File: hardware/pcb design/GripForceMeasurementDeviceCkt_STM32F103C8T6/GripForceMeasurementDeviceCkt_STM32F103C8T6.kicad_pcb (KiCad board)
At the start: 2 copper layers, 60 parts, among them J1 Conn_01x32, J10 Conn_01x32, J11 Conn_01x32, J12 Conn_01x32, J13 Conn_01x32, J2 Conn_01x03, J3 Conn_01x04, J4 Conn_02x03_CC, J5 Conn_01x32, J6 Conn_01x32, J7 Conn_01x32, J8 Conn_01x32, J9 Conn_01x32, P1 USB_C_Plug_USB2.0, U1 STM32F103C8Tx, U10 ADG732BSUZ, U11 ADG732BSUZ, U12 ADG732BSUZ, U13 ADG732BSUZ, U2 FT232RL, U3 ADG732BSUZ, U4 ADG732BSUZ, U5 LM358, U6 ADG732BSUZ, U7 ADG732BSUZ, U8 ADG732BSUZ, U9 ADG732BSUZ, Y1 8MHz

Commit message: complete schemetic design. working on PCB
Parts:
- removed the J10 at (87.5, 145.8)
- removed the J6 at (232.8, 56.5)
- added J14: Conn_01x32, Connector_FFC-FPC:Hirose_FH12-32S-0.5SH_1x32-1MP_P0.50mm_Horizontal, B.Cu at (39.2, 118.1)
- added J15: Conn_01x32, Connector_FFC-FPC:Hirose_FH12-32S-0.5SH_1x32-1MP_P0.50mm_Horizontal, B.Cu at (64.6, 118.1)
- added J16: Conn_01x32, Connector_FFC-FPC:Hirose_FH12-32S-0.5SH_1x32-1MP_P0.50mm_Horizontal, B.Cu at (90.1, 118.1)
- added J17: Conn_01x32, Connector_FFC-FPC:Hirose_FH12-32S-0.5SH_1x32-1MP_P0.50mm_Horizontal, B.Cu at (115.2, 118.1)
- added J19: Power_Conn, Connector_PinHeader_2.54mm:PinHeader_1x03_P2.54mm_Vertical, F.Cu at (35.6, 58.2)
- added J3: TX_Conn, Connector_PinHeader_2.54mm:PinHeader_1x03_P2.54mm_Vertical, F.Cu at (111.3, 65.8)
- added J4: Bluetooth_Module_HLK_B40_(Customized), Connector_PinSocket_2.54mm:PinSocket_1x06_P2.54mm_Vertical, F.Cu at (119.3, 66.9)
- added U1: ESP32-C3-Mini, RF_WiFi:ESP32-C3-Mini-through-hole, F.Cu at (163.1, 65.0)
- C13: renamed from C9; moved to B.Cu
- C14: renamed from C10; moved to B.Cu
- C20: renamed from C24; moved to B.Cu
- C21: renamed from C22; moved to B.Cu
- C22: renamed from C23; moved to B.Cu
- C23: renamed from C21; moved to B.Cu
- C24: renamed from C16; moved to B.Cu
- J1: value Conn_01x32 -> RX_Conn; footprint Connector_FFC-FPC:TE_3-1734839-2_1x32-1MP_P0.5mm_Horizontal -> Connector_PinHeader_2.54mm:PinHeader_1x03_P2.54mm_Vertical
- J10: renamed from J5; footprint Connector_FFC-FPC:TE_3-1734839-2_1x32-1MP_P0.5mm_Horizontal -> Connector_FFC-FPC:Hirose_FH12-32S-0.5SH_1x32-1MP_P0.50mm_Horizontal
- J11, J12, J8, J9: footprint Connector_FFC-FPC:TE_3-1734839-2_1x32-1MP_P0.5mm_Horizontal -> Connector_FFC-FPC:Hirose_FH12-32S-0.5SH_1x32-1MP_P0.50mm_Horizontal
- J13: footprint Connector_FFC-FPC:TE_3-1734839-2_1x32-1MP_P0.5mm_Horizontal -> Connector_FFC-FPC:Hirose_FH12-32S-0.5SH_1x32-1MP_P0.50mm_Horizontal; moved to B.Cu
- J2: renamed from J4; value Conn_02x03_CC -> Boot_Conn
- J5: renamed from J3; value Conn_01x04 -> SWD
- J7: value Conn_01x32 -> Gyro_Sensor_ICM_20948_SparkFun_Module; footprint Connector_FFC-FPC:TE_3-1734839-2_1x32-1MP_P0.5mm_Horizontal -> Connector_PinSocket_2.54mm:PinSocket_1x06_P2.54mm_Vertical
- U10: renamed from U13; moved to B.Cu
- U11, U12: moved to B.Cu
- U13: renamed from U10; moved to B.Cu
- moved D1 244.7 mm to (36.5, 62.2), turned to 180 degrees
- moved U2 241.9 mm to (32.4, 79.5), turned to 90 degrees
- moved U3 241.8 mm to (32.1, 90.4), turned to 90 degrees
- moved RV1 237.6 mm to (39.5, 87.9), turned to 90 degrees
- moved P1 236.6 mm to (27.7, 66.8), turned to -90 degrees
- moved J6 228.2 mm to (26.2, 93.1), turned to 180 degrees
- moved C9 227.6 mm to (40.7, 63.7), turned to -90 degrees
- moved R4 226.1 mm to (45.1, 86.6), turned to -90 degrees
- moved U13 224.3 mm to (39.2, 108.0)
- moved L1 224.3 mm to (45.1, 62.2)
- moved C11 222.2 mm to (44.7, 68.5), turned to 180 degrees
- moved R3 222.1 mm to (34.0, 73.2), turned to 180 degrees
- moved C1 220.2 mm to (30.8, 73.2)
- moved R1 219.9 mm to (37.0, 65.4)
- moved C13 218.1 mm to (66.6, 67.7), turned to 180 degrees
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- renumbered C14 to C1, C11 to C10, C12 to C11, C8 to C12, C20 to C15, C15 to C16, C1 to C2, C2 to C3, C3 to C4, C4 to C5, C5 to C6, C6 to C7, C7 to C8, C13 to C9, J2 to J6, R2 to R1, R1 to R2, U4 to U14, U5 to U3, U1 to U4, U9 to U5, U3 to U6, U6 to U7, U7 to U8, U8 to U9
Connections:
- J1 pad 1: ROW_L_1 -> TX_BTH
- J1 pad 2: ROW_L_2 -> RX
- J1 pad 3: ROW_L_3 -> TX_USB
- J11 pad 1: /COL_R_2.S1 -> /COL_L_2.S17
- J11 pad 10: /COL_R_2.S10 -> /COL_L_2.S26
- J11 pad 11: /COL_R_2.S11 -> /COL_L_2.S27
- J11 pad 12: /COL_R_2.S12 -> /COL_L_2.S28
- J11 pad 13: /COL_R_2.S13 -> /COL_L_2.S29
- J11 pad 14: /COL_R_2.S14 -> /COL_L_2.S30
- J11 pad 15: /COL_R_2.S15 -> /COL_L_2.S31
- J11 pad 16: /COL_R_2.S16 -> /COL_L_2.S32
- J11 pad 17: /COL_R_2.S32 -> /COL_L_2.S16
- J11 pad 18: /COL_R_2.S31 -> /COL_L_2.S15
- J11 pad 19: /COL_R_2.S30 -> /COL_L_2.S14
- J11 pad 2: /COL_R_2.S2 -> /COL_L_2.S18
- J11 pad 20: /COL_R_2.S29 -> /COL_L_2.S13
- J11 pad 21: /COL_R_2.S28 -> /COL_L_2.S12
- J11 pad 22: /COL_R_2.S27 -> /COL_L_2.S11
- J11 pad 23: /COL_R_2.S26 -> /COL_L_2.S10
- J11 pad 24: /COL_R_2.S25 -> /COL_L_2.S9
- J11 pad 25: /COL_R_2.S24 -> /COL_L_2.S8
- J11 pad 26: /COL_R_2.S23 -> /COL_L_2.S7
- J11 pad 27: /COL_R_2.S22 -> /COL_L_2.S6
- J11 pad 28: /COL_R_2.S21 -> /COL_L_2.S5
- J11 pad 29: /COL_R_2.S20 -> /COL_L_2.S4
- J11 pad 3: /COL_R_2.S3 -> /COL_L_2.S19
- J11 pad 30: /COL_R_2.S19 -> /COL_L_2.S3
- J11 pad 31: /COL_R_2.S18 -> /COL_L_2.S2
- J11 pad 32: /COL_R_2.S17 -> /COL_L_2.S1
- J11 pad 4: /COL_R_2.S4 -> /COL_L_2.S20
- J11 pad 5: /COL_R_2.S5 -> /COL_L_2.S21
- J11 pad 6: /COL_R_2.S6 -> /COL_L_2.S22
- J11 pad 7: /COL_R_2.S7 -> /COL_L_2.S23
- J11 pad 8: /COL_R_2.S8 -> /COL_L_2.S24
- J11 pad 9: /COL_R_2.S9 -> /COL_L_2.S25
- J12 pad 1: /COL_R_3.S1 -> /COL_L_3.S17
- J12 pad 10: /COL_R_3.S10 -> /COL_L_3.S26
- J12 pad 11: /COL_R_3.S11 -> /COL_L_3.S27
- J12 pad 12: /COL_R_3.S12 -> /COL_L_3.S28
- J12 pad 13: /COL_R_3.S13 -> /COL_L_3.S29
- J12 pad 14: /COL_R_3.S14 -> /COL_L_3.S30
- J12 pad 15: /COL_R_3.S15 -> /COL_L_3.S31
- J12 pad 16: /COL_R_3.S16 -> /COL_L_3.S32
- J12 pad 17: /COL_R_3.S32 -> /COL_L_3.S16
- J12 pad 18: /COL_R_3.S31 -> /COL_L_3.S15
- J12 pad 19: /COL_R_3.S30 -> /COL_L_3.S14
- J12 pad 2: /COL_R_3.S2 -> /COL_L_3.S18
- J12 pad 20: /COL_R_3.S29 -> /COL_L_3.S13
- J12 pad 21: /COL_R_3.S28 -> /COL_L_3.S12
- J12 pad 22: /COL_R_3.S27 -> /COL_L_3.S11
- J12 pad 23: /COL_R_3.S26 -> /COL_L_3.S10
- J12 pad 24: /COL_R_3.S25 -> /COL_L_3.S9
- J12 pad 25: /COL_R_3.S24 -> /COL_L_3.S8
- J12 pad 26: /COL_R_3.S23 -> /COL_L_3.S7
- J12 pad 27: /COL_R_3.S22 -> /COL_L_3.S6
- J12 pad 28: /COL_R_3.S21 -> /COL_L_3.S5
- J12 pad 29: /COL_R_3.S20 -> /COL_L_3.S4
- J12 pad 3: /COL_R_3.S3 -> /COL_L_3.S19
- J12 pad 30: /COL_R_3.S19 -> /COL_L_3.S3
- J12 pad 31: /COL_R_3.S18 -> /COL_L_3.S2
- J12 pad 32: /COL_R_3.S17 -> /COL_L_3.S1
- J12 pad 4: /COL_R_3.S4 -> /COL_L_3.S20
- J12 pad 5: /COL_R_3.S5 -> /COL_L_3.S21
- J12 pad 6: /COL_R_3.S6 -> /COL_L_3.S22
- J12 pad 7: /COL_R_3.S7 -> /COL_L_3.S23
- J12 pad 8: /COL_R_3.S8 -> /COL_L_3.S24
- J12 pad 9: /COL_R_3.S9 -> /COL_L_3.S25
- J13 pad 1: /COL_R_4.S1 -> /COL_R_4.S17
- J13 pad 10: /COL_R_4.S10 -> /COL_R_4.S26
- J13 pad 11: /COL_R_4.S11 -> /COL_R_4.S27
- J13 pad 12: /COL_R_4.S12 -> /COL_R_4.S28
- J13 pad 13: /COL_R_4.S13 -> /COL_R_4.S29
- J13 pad 14: /COL_R_4.S14 -> /COL_R_4.S30
- J13 pad 15: /COL_R_4.S15 -> /COL_R_4.S31
- J13 pad 16: /COL_R_4.S16 -> /COL_R_4.S32
- J13 pad 17: /COL_R_4.S32 -> /COL_R_4.S16
- J13 pad 18: /COL_R_4.S31 -> /COL_R_4.S15
- J13 pad 19: /COL_R_4.S30 -> /COL_R_4.S14
- J13 pad 2: /COL_R_4.S2 -> /COL_R_4.S18
- J13 pad 20: /COL_R_4.S29 -> /COL_R_4.S13
- J13 pad 21: /COL_R_4.S28 -> /COL_R_4.S12
- J13 pad 22: /COL_R_4.S27 -> /COL_R_4.S11
- J13 pad 23: /COL_R_4.S26 -> /COL_R_4.S10
- J13 pad 24: /COL_R_4.S25 -> /COL_R_4.S9
- J13 pad 25: /COL_R_4.S24 -> /COL_R_4.S8
- J13 pad 26: /COL_R_4.S23 -> /COL_R_4.S7
- J13 pad 27: /COL_R_4.S22 -> /COL_R_4.S6
- J13 pad 28: /COL_R_4.S21 -> /COL_R_4.S5
- J13 pad 29: /COL_R_4.S20 -> /COL_R_4.S4
- J13 pad 3: /COL_R_4.S3 -> /COL_R_4.S19
- J13 pad 30: /COL_R_4.S19 -> /COL_R_4.S3
- J13 pad 31: /COL_R_4.S18 -> /COL_R_4.S2
- J13 pad 32: /COL_R_4.S17 -> /COL_R_4.S1
- J13 pad 4: /COL_R_4.S4 -> /COL_R_4.S20
- J13 pad 5: /COL_R_4.S5 -> /COL_R_4.S21
- J13 pad 6: /COL_R_4.S6 -> /COL_R_4.S22
- J13 pad 7: /COL_R_4.S7 -> /COL_R_4.S23
- J13 pad 8: /COL_R_4.S8 -> /COL_R_4.S24
- J13 pad 9: /COL_R_4.S9 -> /COL_R_4.S25
- J7 pad 1: /COL_L_3.S1 -> +5V
- J7 pad 2: /COL_L_3.S2 -> GND
- J7 pad 3: /COL_L_3.S3 -> MOSI
- J7 pad 4: /COL_L_3.S4 -> SCLK
- J7 pad 5: /COL_L_3.S5 -> MISO
- J7 pad 6: /COL_L_3.S6 -> CS-GYRO
- J8 pad 1: /COL_L_4.S1 -> /COL_L_4.S17
- J8 pad 10: /COL_L_4.S10 -> /COL_L_4.S26
- J8 pad 11: /COL_L_4.S11 -> /COL_L_4.S27
- J8 pad 12: /COL_L_4.S12 -> /COL_L_4.S28
- J8 pad 13: /COL_L_4.S13 -> /COL_L_4.S29
- J8 pad 14: /COL_L_4.S14 -> /COL_L_4.S30
- J8 pad 15: /COL_L_4.S15 -> /COL_L_4.S31
- J8 pad 16: /COL_L_4.S16 -> /COL_L_4.S32
- J8 pad 17: /COL_L_4.S32 -> /COL_L_4.S16
- J8 pad 18: /COL_L_4.S31 -> /COL_L_4.S15
- J8 pad 19: /COL_L_4.S30 -> /COL_L_4.S14
- J8 pad 2: /COL_L_4.S2 -> /COL_L_4.S18
- J8 pad 20: /COL_L_4.S29 -> /COL_L_4.S13
- J8 pad 21: /COL_L_4.S28 -> /COL_L_4.S12
- J8 pad 22: /COL_L_4.S27 -> /COL_L_4.S11
- J8 pad 23: /COL_L_4.S26 -> /COL_L_4.S10
- J8 pad 24: /COL_L_4.S25 -> /COL_L_4.S9
- J8 pad 25: /COL_L_4.S24 -> /COL_L_4.S8
- J8 pad 26: /COL_L_4.S23 -> /COL_L_4.S7
- J8 pad 27: /COL_L_4.S22 -> /COL_L_4.S6
- J8 pad 28: /COL_L_4.S21 -> /COL_L_4.S5
- J8 pad 29: /COL_L_4.S20 -> /COL_L_4.S4
- J8 pad 3: /COL_L_4.S3 -> /COL_L_4.S19
- J8 pad 30: /COL_L_4.S19 -> /COL_L_4.S3
- J8 pad 31: /COL_L_4.S18 -> /COL_L_4.S2
- J8 pad 32: /COL_L_4.S17 -> /COL_L_4.S1
- J8 pad 4: /COL_L_4.S4 -> /COL_L_4.S20
- J8 pad 5: /COL_L_4.S5 -> /COL_L_4.S21
- J8 pad 6: /COL_L_4.S6 -> /COL_L_4.S22
- J8 pad 7: /COL_L_4.S7 -> /COL_L_4.S23
- J8 pad 8: /COL_L_4.S8 -> /COL_L_4.S24
- J8 pad 9: /COL_L_4.S9 -> /COL_L_4.S25
- J9 pad 1: /COL_R_1.S1 -> ROW_L_17
- J9 pad 10: /COL_R_1.S10 -> ROW_L_26
- J9 pad 11: /COL_R_1.S11 -> ROW_L_27
- J9 pad 12: /COL_R_1.S12 -> ROW_L_28
- J9 pad 13: /COL_R_1.S13 -> ROW_L_29
- J9 pad 14: /COL_R_1.S14 -> ROW_L_30
- J9 pad 15: /COL_R_1.S15 -> ROW_L_31
- J9 pad 16: /COL_R_1.S16 -> ROW_L_32
- J9 pad 17: /COL_R_1.S32 -> ROW_L_16
- J9 pad 18: /COL_R_1.S31 -> ROW_L_15
- J9 pad 19: /COL_R_1.S30 -> ROW_L_14
- J9 pad 2: /COL_R_1.S2 -> ROW_L_18
- J9 pad 20: /COL_R_1.S29 -> ROW_L_13
- J9 pad 21: /COL_R_1.S28 -> ROW_L_12
- J9 pad 22: /COL_R_1.S27 -> ROW_L_11
- J9 pad 23: /COL_R_1.S26 -> ROW_L_10
- J9 pad 24: /COL_R_1.S25 -> ROW_L_9
- J9 pad 25: /COL_R_1.S24 -> ROW_L_8
- J9 pad 26: /COL_R_1.S23 -> ROW_L_7
- J9 pad 27: /COL_R_1.S22 -> ROW_L_6
- J9 pad 28: /COL_R_1.S21 -> ROW_L_5
- J9 pad 29: /COL_R_1.S20 -> ROW_L_4
- J9 pad 3: /COL_R_1.S3 -> ROW_L_19
- J9 pad 30: /COL_R_1.S19 -> ROW_L_3
- J9 pad 31: /COL_R_1.S18 -> ROW_L_2
- J9 pad 32: /COL_R_1.S17 -> ROW_L_1
- J9 pad 4: /COL_R_1.S4 -> ROW_L_20
- J9 pad 5: /COL_R_1.S5 -> ROW_L_21
- J9 pad 6: /COL_R_1.S6 -> ROW_L_22
- J9 pad 7: /COL_R_1.S7 -> ROW_L_23
- J9 pad 8: /COL_R_1.S8 -> ROW_L_24
- J9 pad 9: /COL_R_1.S9 -> ROW_L_25
- U2 pad 1: TX -> TX_USB
- U2 pad 5: RX -> RX_USB
- U4 pad 14: NSS -> NSS-STM32
- U4 pad 15: SCK -> SCLK
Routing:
- net GND: track 0.00 -> 34.5 mm
- net Net-(D1-A): track 0.00 -> 16.6 mm
- net /COL_R_2.S17: track 0.00 -> 14.5 mm
- net /COL_L_2.S1: track 0.00 -> 14.5 mm
- net /COL_L_3.S17: track 0.00 -> 14.5 mm
- net /COL_L_1.S17: track 0.00 -> 14.5 mm
- net /COL_R_3.S17: track 0.00 -> 14.5 mm
- net /COL_L_4.S17: track 0.00 -> 14.5 mm
- net ROW_R_17: track 0.00 -> 14.5 mm
- net ROW_L_1: track 0.00 -> 14.5 mm
- net /COL_R_1.S17: track 0.00 -> 14.5 mm
- net /COL_L_1.S1: track 0.00 -> 14.5 mm
- net /COL_L_3.S1: track 0.00 -> 14.5 mm
- net /COL_R_1.S1: track 0.00 -> 14.4 mm
- net /COL_R_3.S1: track 0.00 -> 14.4 mm
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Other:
- board outline added: 136 x 70 mm
- board text added: "5V"
- board text added: "A"
- board text added: "A : Amplified"
- board text added: "ADC"
- board text added: "GND"
- board text added: "Gain Controller"
- board text added: "NA"
- board text added: "NA : No Amplification"
- board text added: "X"

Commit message: updated PCB design
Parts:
- added SW1: SW_Push, Button_Switch_SMD:SW_Tactile_SPST_NO_Straight_CK_PTS636Sx25SMTRLFS, F.Cu at (52.9, 61.8)
- C12, C2, C3, C4, C5, C6, C7, C8, FB1, R2: moved to B.Cu
- J2: value Boot_Conn -> Boot Conn
- moved J6 66.2 mm to (86.2, 65.2), turned to 0 degrees
- moved R4 64.1 mm to (105.1, 63.9)
- moved RV1 64.1 mm to (99.5, 65.2)
- moved U3 64.1 mm to (92.1, 67.6)
- moved J2 51.3 mm to (50.6, 69.4)
- moved C4 30.4 mm to (62.5, 73.1), turned to 90 degrees
- moved U1 28.4 mm to (142.6, 84.6), turned to 180 degrees
- moved R2 26.3 mm to (64.3, 78.4), turned to 0 degrees
- moved C3 26.0 mm to (63.3, 70.5), turned to 0 degrees
- moved U4 21.4 mm to (64.4, 72.0), turned to 180 degrees
- moved C5 20.5 mm to (65.2, 73.8), turned to 180 degrees
- moved C13 13.7 mm to (78.4, 74.5), turned to 0 degrees
- moved C14 12.2 mm to (78.4, 69.5), turned to 0 degrees
- moved C2 10.9 mm to (71.6, 74.8), turned to 0 degrees
- moved Y1 10.4 mm to (76.4, 74.5), turned to 90 degrees
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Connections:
- net Net-(P1-D+) renamed /D+
- net Net-(P1-D-) renamed /D-
- J2 pad 2: BOOT1 -> +3.3V
- J2 pad 3: GND -> BOOT1
- J2 pad 4: GND -> /SW_BOOT0
- J2 pad 5: /SW_BOOT0 -> GND
- J2 pad 6: +3.3V -> GND
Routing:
- net GND: track 34.5 -> 613.6 mm, vias 0 -> 14
- net +5V: track 6.27 -> 316.8 mm, vias 0 -> 9
- net L4: track 0.00 -> 245.3 mm, vias 0 -> 10
- net L0: track 0.00 -> 231.1 mm, vias 0 -> 5
- net L3: track 0.00 -> 227.2 mm, vias 0 -> 11
- net L2: track 0.00 -> 210.8 mm, vias 0 -> 11
- net ADG_EN: track 0.00 -> 205.5 mm, vias 0 -> 11
- net L1: track 0.00 -> 201.9 mm, vias 0 -> 10
- net ADG_WR: track 0.00 -> 198.3 mm, vias 0 -> 11
- net SENSOR_OUT: track 0.00 -> 126.9 mm, vias 0 -> 5
- net COL_SEL_L_4: track 0.00 -> 116.0 mm, vias 0 -> 2
- net COL_SEL_R_4: track 0.00 -> 108.3 mm, vias 0 -> 2
- net RX_USB: track 0.00 -> 95.4 mm, vias 0 -> 1
- net TX_USB: track 0.00 -> 91.8 mm, vias 0 -> 1
- net MOSI: track 0.00 -> 91.7 mm
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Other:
- board text added: "- Gyro Should be in the middle"
- board text added: "- Multiplexers and sockets are placed such a way so that"
- board text added: "0"
- board text added: "1"
- board text added: "3V3"
- board text added: "BOOT0"
- board text added: "BOOT1"
- board text added: "CS"
- board text added: "GYRO_ICM_20948_Module"
- board text added: "MISO"
- board text added: "MOSI"
- board text added: "NL"
- board text added: "Note:"
- board text added: "RX"
- board text added: "RX_B"
- board text added: "RX_U"
- board text added: "SCLK"
- board text added: "SWCLK"
- board text added: "SWO"
- board text added: "TX"
- board text added: "TX_B"
- board text added: "TX_U"
- board text added: "these match with the sensor pad"

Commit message: some photos added
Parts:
- moved J7 0.69 mm to (155.8, 82.7)
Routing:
- net +5V: track 316.8 -> 546.2 mm, vias 9 -> 19
- net GND: track 613.6 -> 761.1 mm, vias 14 -> 23
- net MISO: track 67.0 -> 125.8 mm
- net SCLK: track 67.3 -> 113.9 mm
- net CS-GYRO: track 0.00 -> 42.5 mm
- net MOSI: track 91.7 -> 124.8 mm
- net ESP_SELECT: track 14.4 -> 0.00 mm, vias 1 -> 0
- net SENSOR_OUT: track 126.9 -> 127.6 mm, vias 5 -> 4
- net COL_SEL_R_4: vias 2 -> 1
- net COL_SEL_R_1: vias 4 -> 3
- net COL_SEL_L_2: vias 3 -> 2

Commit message: pcb trace complete
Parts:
- moved C10 31.5 mm to (75.9, 63.6)
- moved C12 31.5 mm to (103.1, 71.8)
- moved C14 31.5 mm to (109.9, 68.5)
- moved C15 31.5 mm to (179.1, 102.8)
- moved C20 31.5 mm to (164.6, 102.8)
- moved C24 31.5 mm to (139.5, 102.9)
- moved C6 31.5 mm to (103.1, 68.2)
- moved C8 31.5 mm to (103.1, 66.4)
- moved FB1 31.5 mm to (103.4, 64.2)
- moved J13 31.5 mm to (171.8, 117.0)
- moved J5 31.5 mm to (93.0, 60.6)
- moved J6 31.5 mm to (117.7, 64.2)
- moved J8 31.5 mm to (171.8, 117.0)
- moved R2 31.5 mm to (95.8, 77.3)
- moved RV1 31.5 mm to (131.0, 64.1)
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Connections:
- U1 pad 10: SCLK -> MOSI
- U1 pad 12: unconnected-(U1-GP8-Pad12) -> SCLK
- U1 pad 13: unconnected-(U1-GP9-Pad13) -> NSS-STM32
- U1 pad 14: NSS-STM32 -> unconnected-(U1-GP10-Pad14)
- U1 pad 6: MOSI -> unconnected-(U1-GP2-Pad6)
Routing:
- net MOSI: track 124.8 -> 115.0 mm
- net SCLK: track 113.9 -> 111.7 mm, vias 2 -> 0
- net NSS-STM32: track 69.2 -> 67.1 mm
- net CS-GYRO: track 42.5 -> 44.4 mm
- net unconnected-(U1-GP10-Pad14): track 0.00 -> 1.86 mm

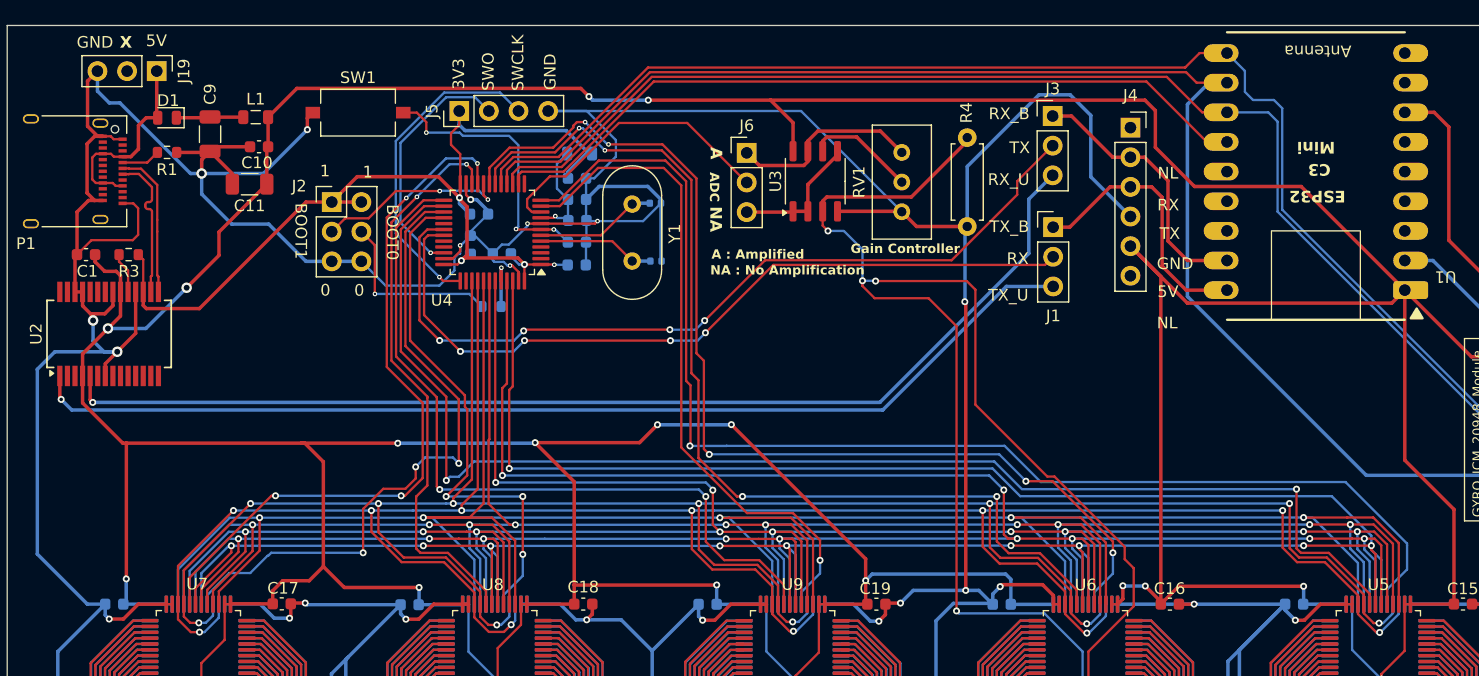
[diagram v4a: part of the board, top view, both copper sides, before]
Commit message: re-configured the pins connection again
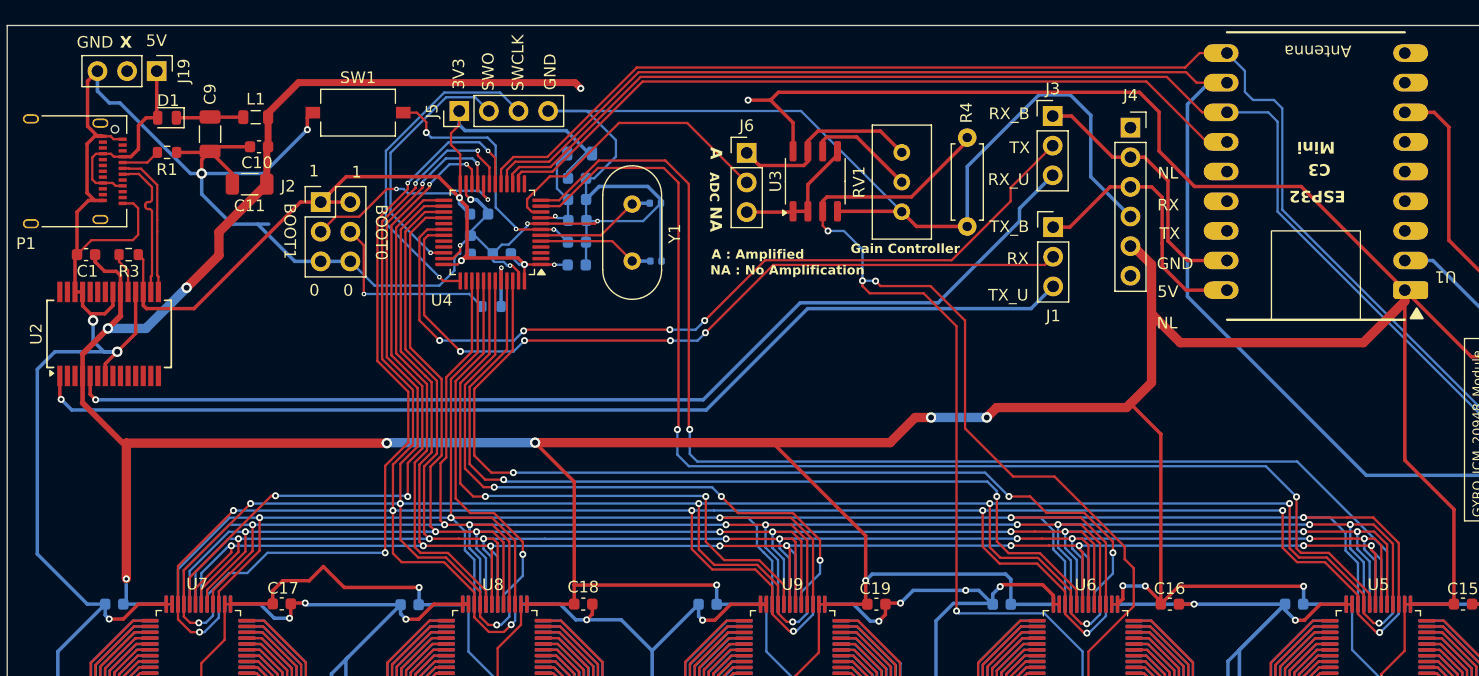
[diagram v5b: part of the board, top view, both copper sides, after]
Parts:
- moved J2 0.95 mm to (81.2, 68.4)
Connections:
- U4 pad 11: COL_SEL_R_3 -> COL_SEL_L_4
- U4 pad 18: ROW_SEL_L -> COL_SEL_R_1
- U4 pad 19: ROW_SEL_R -> ADG_EN
- U4 pad 21: COL_SEL_L_1 -> ADG_WR
- U4 pad 22: COL_SEL_L_2 -> COL_SEL_L_1
- U4 pad 25: COL_SEL_L_3 -> COL_SEL_L_2
- U4 pad 26: COL_SEL_L_4 -> L4
- U4 pad 27: COL_SEL_R_1 -> L3
- U4 pad 28: COL_SEL_R_2 -> L2
- U4 pad 39: ADG_WR -> L1
- U4 pad 40: ADG_EN -> L0
- U4 pad 41: L0 -> COL_SEL_R_2
- U4 pad 42: L1 -> COL_SEL_L_3
- U4 pad 43: L2 -> COL_SEL_R_3
- U4 pad 45: L3 -> ROW_SEL_L
- U4 pad 46: L4 -> ROW_SEL_R
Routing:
- net L4: track 245.3 -> 185.3 mm, vias 10 -> 9
- net L3: track 227.2 -> 193.9 mm, vias 11 -> 9
- net GND: track 761.1 -> 731.0 mm, vias 23 -> 22
- net ADG_EN: track 205.5 -> 225.2 mm, vias 11 -> 12
- net ADG_WR: track 198.3 -> 215.1 mm, vias 11 -> 12
- net COL_SEL_R_2: track 45.2 -> 33.0 mm, vias 3 -> 1
- net COL_SEL_L_3: track 65.9 -> 53.7 mm
- net COL_SEL_L_4: track 116.0 -> 104.8 mm
- net ROW_SEL_R: track 90.7 -> 80.1 mm, vias 5 -> 3
- net L2: track 210.8 -> 201.4 mm, vias 11 -> 9
- net ROW_SEL_L: track 86.1 -> 77.3 mm, vias 4 -> 2
- net COL_SEL_R_1: track 56.0 -> 63.9 mm
- net +5V: track 546.2 -> 553.8 mm
- net COL_SEL_L_2: track 48.6 -> 42.8 mm, vias 2 -> 0
- net L0: track 231.1 -> 226.5 mm
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
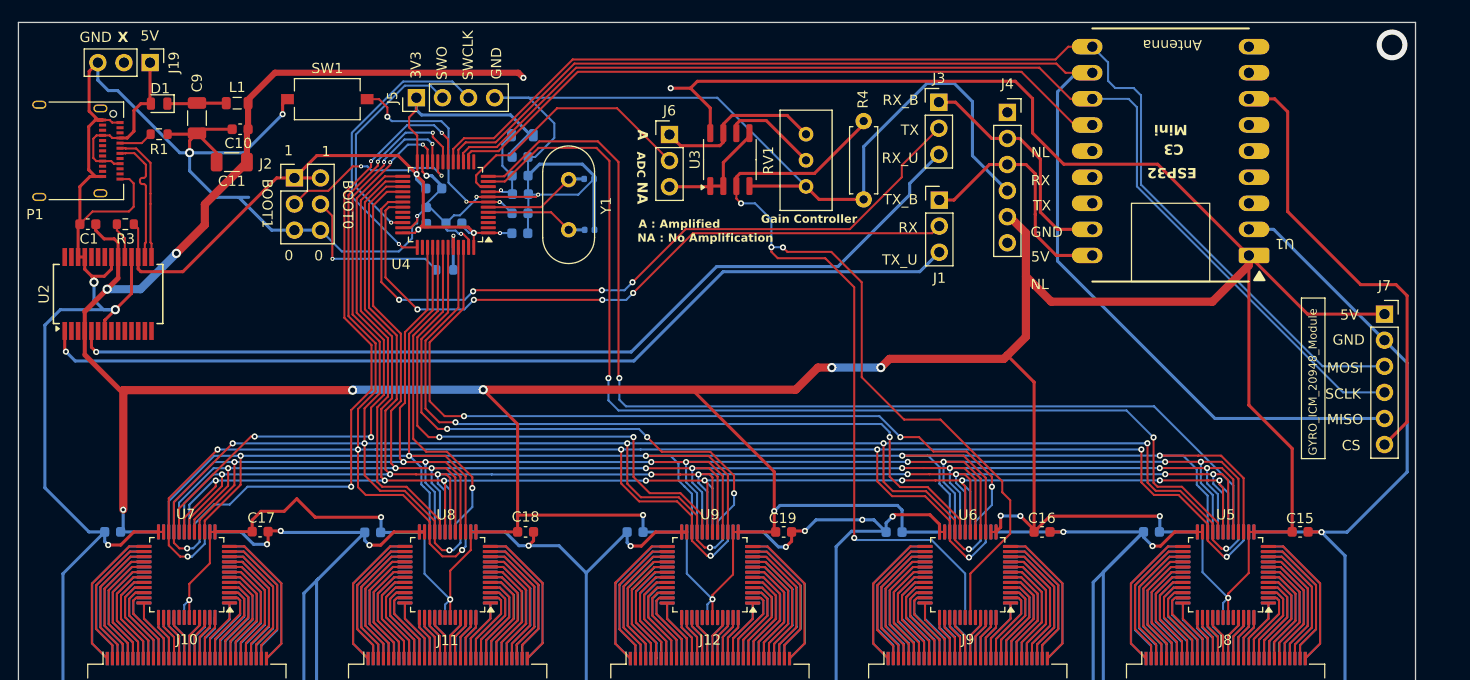
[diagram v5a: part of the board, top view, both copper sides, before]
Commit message: bluetooth module has removed
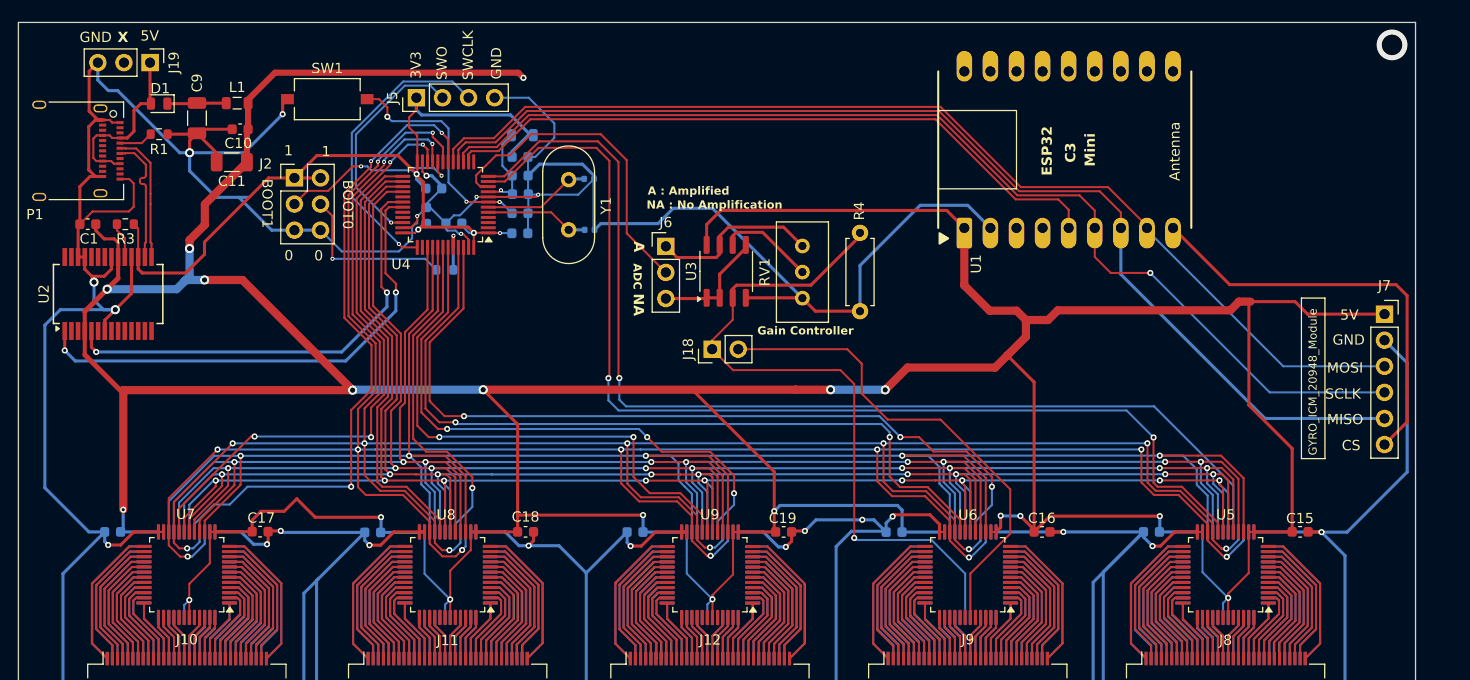
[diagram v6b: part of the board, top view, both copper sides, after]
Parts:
- removed J1: RX_Conn, Connector_PinHeader_2.54mm:PinHeader_1x03_P2.54mm_Vertical
- removed J3: TX_Conn, Connector_PinHeader_2.54mm:PinHeader_1x03_P2.54mm_Vertical
- removed J4: Bluetooth_Module_HLK_B40_(Customized), Connector_PinSocket_2.54mm:PinSocket_1x06_P2.54mm_Vertical
- added J18: Conn_01x02, Connector_PinHeader_2.54mm:PinHeader_1x02_P2.54mm_Vertical, F.Cu at (121.8, 85.1)
- moved U1 36.8 mm to (138.8, 73.3), turned to 90 degrees
- moved J6 10.9 mm to (117.3, 75.0)
- moved R4 10.9 mm to (136.2, 73.7)
- moved RV1 10.9 mm to (130.6, 75.0)
- moved U3 10.9 mm to (123.2, 77.5)
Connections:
- R4 pad 1: SENSOR_OUT -> SENSOR_OUT_R
- U1 pad 10: MOSI -> unconnected-(U1-GP6-Pad10)
- U1 pad 11: MISO -> unconnected-(U1-GP7-Pad11)
- U1 pad 12: SCLK -> unconnected-(U1-GP8-Pad12)
- U1 pad 13: NSS-STM32 -> unconnected-(U1-GP9-Pad13)
- U1 pad 5: unconnected-(U1-GP1-Pad5) -> NSS-STM32
- U1 pad 6: unconnected-(U1-GP2-Pad6) -> SCLK
- U1 pad 7: CS-GYRO -> MISO
- U1 pad 8: unconnected-(U1-GP4-Pad8) -> MOSI
- U1 pad 9: unconnected-(U1-GP5-Pad9) -> CS-GYRO
- U14 pad 43: SENSOR_OUT -> SENSOR_OUT_R
- U2 pad 1: TX_USB -> RX
- U2 pad 5: RX_USB -> TX
- U3 pad 3: SENSOR_OUT -> SENSOR_OUT_R
- U6 pad 43: SENSOR_OUT -> SENSOR_OUT_L
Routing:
- net SENSOR_OUT: track 127.2 -> 0.00 mm, vias 4 -> 0
- net RX_USB: track 92.9 -> 0.00 mm, vias 1 -> 0
- net TX_USB: track 91.8 -> 0.00 mm, vias 1 -> 0
- net SENSOR_OUT_R: track 0.00 -> 68.3 mm, vias 0 -> 1
- net SENSOR_OUT_L: track 0.00 -> 47.9 mm
- net GND: track 731.0 -> 695.5 mm
- net TX: track 72.1 -> 44.5 mm, vias 4 -> 2
- net +5V: track 553.8 -> 527.5 mm
- net TX_BTH: track 23.5 -> 0.00 mm
- net RX_BTH: track 23.1 -> 0.00 mm
- net RX: track 66.9 -> 48.6 mm, vias 4 -> 2
- net MISO: track 125.5 -> 108.8 mm
- net MOSI: track 115.0 -> 104.3 mm
- net ADC: track 25.7 -> 31.9 mm
- net SCLK: track 111.7 -> 106.0 mm, vias 0 -> 1
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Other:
- board text removed: "NL"
- board text removed: "RX"
- board text removed: "RX_B"
- board text removed: "RX_U"
- board text removed: "TX"
- board text removed: "TX_B"
- board text removed: "TX_U"
